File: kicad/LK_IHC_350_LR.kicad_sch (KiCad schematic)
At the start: 27 parts, among them Q1 BTA12-700SW, U1 LS7631, U2 PC123

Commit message: fix spelling mistake in kicad project name
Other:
- title: LK ICH Dimmer 350 LR -> LK IHC Dimmer 350 LR
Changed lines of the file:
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@@
   (paper "A4")
   (title_block
-    (title "LK ICH Dimmer 350 LR")
+    (title "LK IHC Dimmer 350 LR")
     (date "2023-12-18")
-    (rev "4")
+    (rev "5")
     (comment 1 "LK913CB4")
     (comment 2 "LK913A4")
@@
     (pin "1")
     (instances
-      (project "LK_ICH_350LR"
+      (project "LK_IHC_350_LR"
         (path "/00661e67-d895-4a4d-8f6d-597ae5750c96"
           (reference "R5") (unit 1)
@@
     (pin "2")
     (instances
-      (project "LK_ICH_350LR"
+      (project "LK_IHC_350_LR"
         (path "/00661e67-d895-4a4d-8f6d-597ae5750c96"
           (reference "C6") (unit 1)
@@
     (pin "2")
     (instances
-      (project "LK_ICH_350LR"
+      (project "LK_IHC_350_LR"
         (path "/00661e67-d895-4a4d-8f6d-597ae5750c96"
           (reference "C5") (unit 1)
@@
     (pin "1")
     (instances
-      (project "LK_ICH_350LR"
+      (project "LK_IHC_350_LR"
         (path "/00661e67-d895-4a4d-8f6d-597ae5750c96"
           (reference "R7") (unit 1)
@@
     (pin "1")
     (instances
-      (project "LK_ICH_350LR"
+      (project "LK_IHC_350_LR"
         (path "/00661e67-d895-4a4d-8f6d-597ae5750c96"
           (reference "R6") (unit 1)
@@
     (pin "2")
     (instances
-      (project "LK_ICH_350LR"
+      (project "LK_IHC_350_LR"
         (path "/00661e67-d895-4a4d-8f6d-597ae5750c96"
           (reference "C7") (unit 1)
@@
     (pin "1")
     (instances
-      (project "LK_ICH_350LR"
+      (project "LK_IHC_350_LR"
         (path "/00661e67-d895-4a4d-8f6d-597ae5750c96"
           (reference "J1") (unit 1)
@@
     (pin "1")
     (instances
-      (project "LK_ICH_350LR"
+      (project "LK_IHC_350_LR"
         (path "/00661e67-d895-4a4d-8f6d-597ae5750c96"
           (reference "#PWR02") (unit 1)
@@
     (pin "1")
     (instances
-      (project "LK_ICH_350LR"
+      (project "LK_IHC_350_LR"
         (path "/00661e67-d895-4a4d-8f6d-597ae5750c96"
           (reference "D1") (unit 1)
@@
     (pin "2")
     (instances
-      (project "LK_ICH_350LR"
+      (project "LK_IHC_350_LR"
         (path "/00661e67-d895-4a4d-8f6d-597ae5750c96"
           (reference "D5") (unit 1)
@@
     (pin "1")
     (instances
-      (project "LK_ICH_350LR"
+      (project "LK_IHC_350_LR"
         (path "/00661e67-d895-4a4d-8f6d-597ae5750c96"
           (reference "J2") (unit 1)
@@
     (pin "2")
     (instances
-      (project "LK_ICH_350LR"
+      (project "LK_IHC_350_LR"
         (path "/00661e67-d895-4a4d-8f6d-597ae5750c96"
           (reference "Q1") (unit 1)
@@
     (pin "1")
     (instances
-      (project "LK_ICH_350LR"
+      (project "LK_IHC_350_LR"
         (path "/00661e67-d895-4a4d-8f6d-597ae5750c96"
           (reference "#PWR04") (unit 1)
@@
     (pin "1")
     (instances
-      (project "LK_ICH_350LR"
+      (project "LK_IHC_350_LR"
         (path "/00661e67-d895-4a4d-8f6d-597ae5750c96"
           (reference "F1") (unit 1)
@@
     (pin "1")
     (instances
-      (project "LK_ICH_350LR"
+      (project "LK_IHC_350_LR"
         (path "/00661e67-d895-4a4d-8f6d-597ae5750c96"
           (reference "L1") (unit 1)
@@
     (pin "1")
     (instances
-      (project "LK_ICH_350LR"
+      (project "LK_IHC_350_LR"
         (path "/00661e67-d895-4a4d-8f6d-597ae5750c96"
           (reference "R4") (unit 1)
@@
     (pin "1")
     (instances
-      (project "LK_ICH_350LR"
+      (project "LK_IHC_350_LR"
         (path "/00661e67-d895-4a4d-8f6d-597ae5750c96"
           (reference "#PWR06") (unit 1)
@@
     (pin "1")
     (instances
-      (project "LK_ICH_350LR"
+      (project "LK_IHC_350_LR"
         (path "/00661e67-d895-4a4d-8f6d-597ae5750c96"
           (reference "#PWR01") (unit 1)
@@
     (pin "1")
     (instances
-      (project "LK_ICH_350LR"
+      (project "LK_IHC_350_LR"
         (path "/00661e67-d895-4a4d-8f6d-597ae5750c96"
           (reference "#PWR05") (unit 1)
@@
     (pin "1")
     (instances
-      (project "LK_ICH_350LR"
+      (project "LK_IHC_350_LR"
         (path "/00661e67-d895-4a4d-8f6d-597ae5750c96"
           (reference "#PWR03") (unit 1)
@@
     (pin "1")
     (instances
-      (project "LK_ICH_350LR"
+      (project "LK_IHC_350_LR"
         (path "/00661e67-d895-4a4d-8f6d-597ae5750c96"
           (reference "VR1") (unit 1)
@@
     (pin "1")
     (instances
-      (project "LK_ICH_350LR"
+      (project "LK_IHC_350_LR"
         (path "/00661e67-d895-4a4d-8f6d-597ae5750c96"
           (reference "CR1") (unit 1)
@@
     (pin "2")
     (instances
-      (project "LK_ICH_350LR"
+      (project "LK_IHC_350_LR"
         (path "/00661e67-d895-4a4d-8f6d-597ae5750c96"
           (reference "C3") (unit 1)
@@
     (pin "1")
     (instances
-      (project "LK_ICH_350LR"
+      (project "LK_IHC_350_LR"
         (path "/00661e67-d895-4a4d-8f6d-597ae5750c96"
           (reference "#PWR08") (unit 1)
@@
     (pin "1")
     (instances
-      (project "LK_ICH_350LR"
+      (project "LK_IHC_350_LR"
         (path "/00661e67-d895-4a4d-8f6d-597ae5750c96"
           (reference "R3") (unit 1)
@@
     (pin "1")
     (instances
-      (project "LK_ICH_350LR"
+      (project "LK_IHC_350_LR"
         (path "/00661e67-d895-4a4d-8f6d-597ae5750c96"
           (reference "R1") (unit 1)
@@
     (pin "1")
     (instances
-      (project "LK_ICH_350LR"
+      (project "LK_IHC_350_LR"
         (path "/00661e67-d895-4a4d-8f6d-597ae5750c96"
           (reference "R8") (unit 1)
@@
     (pin "4")
     (instances
-      (project "LK_ICH_350LR"
+      (project "LK_IHC_350_LR"
         (path "/00661e67-d895-4a4d-8f6d-597ae5750c96"
           (reference "U1") (unit 1)
@@
     (pin "2")
     (instances
-      (project "LK_ICH_350LR"
+      (project "LK_IHC_350_LR"
         (path "/00661e67-d895-4a4d-8f6d-597ae5750c96"
           (reference "C4") (unit 1)
@@
     (pin "1")
     (instances
-      (project "LK_ICH_350LR"
+      (project "LK_IHC_350_LR"
         (path "/00661e67-d895-4a4d-8f6d-597ae5750c96"
           (reference "LA1") (unit 1)
@@
     (pin "1")
     (instances
-      (project "LK_ICH_350LR"
+      (project "LK_IHC_350_LR"
         (path "/00661e67-d895-4a4d-8f6d-597ae5750c96"
           (reference "R2") (unit 1)
@@
     (pin "2")
     (instances
-      (project "LK_ICH_350LR"
+      (project "LK_IHC_350_LR"
         (path "/00661e67-d895-4a4d-8f6d-597ae5750c96"
           (reference "C1") (unit 1)
@@
     (pin "1")
     (instances
-      (project "LK_ICH_350LR"
+      (project "LK_IHC_350_LR"
         (path "/00661e67-d895-4a4d-8f6d-597ae5750c96"
           (reference "#PWR07") (unit 1)
@@
     (pin "3")
     (instances
-      (project "LK_ICH_350LR"
+      (project "LK_IHC_350_LR"
         (path "/00661e67-d895-4a4d-8f6d-597ae5750c96"
           (reference "U2") (unit 1)
@@
     (pin "2")
     (instances
-      (project "LK_ICH_350LR"
+      (project "LK_IHC_350_LR"
         (path "/00661e67-d895-4a4d-8f6d-597ae5750c96"
           (reference "C2") (unit 1)

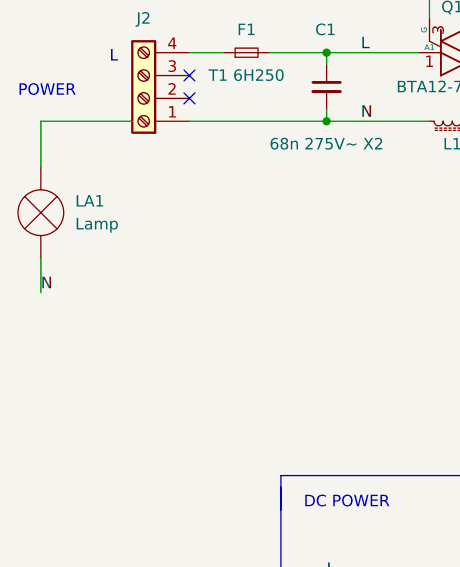
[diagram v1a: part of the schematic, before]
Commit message: replace N schematic label with plain text label on net not N
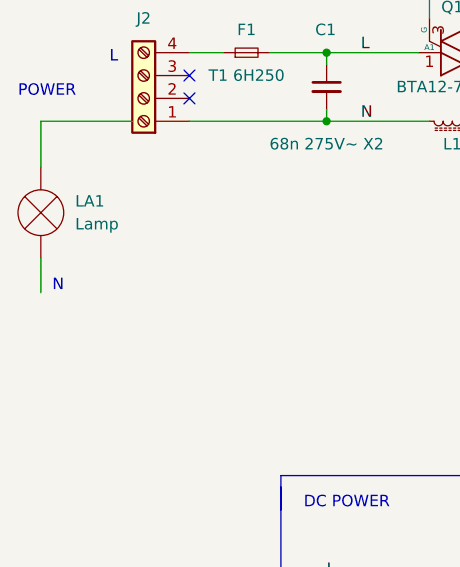
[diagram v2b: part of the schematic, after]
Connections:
- net N: no longer LA1.1 (-)
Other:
- note added: "N"
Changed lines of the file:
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@@
+    (effects (font (size 1.27 1.27)) (justify left bottom))
+  )
+  (text "N" (at 54.61 129.54 0)
     (effects (font (size 1.27 1.27)) (justify left bottom))
   )
@@
     (effects (font (size 1.27 1.27)) (justify left bottom))
   )
-  (label "N" (at 53.34 129.5355 0) (fields_autoplaced)
-    (effects (font (size 1.27 1.27)) (justify left bottom))
-  )
